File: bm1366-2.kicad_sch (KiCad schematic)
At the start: 73 parts, among them U1 25MHz, U13 BM1368_mode0, U15 TLV3544, U16 AP7331, U17 AP7331, U18 BM1368_mode0

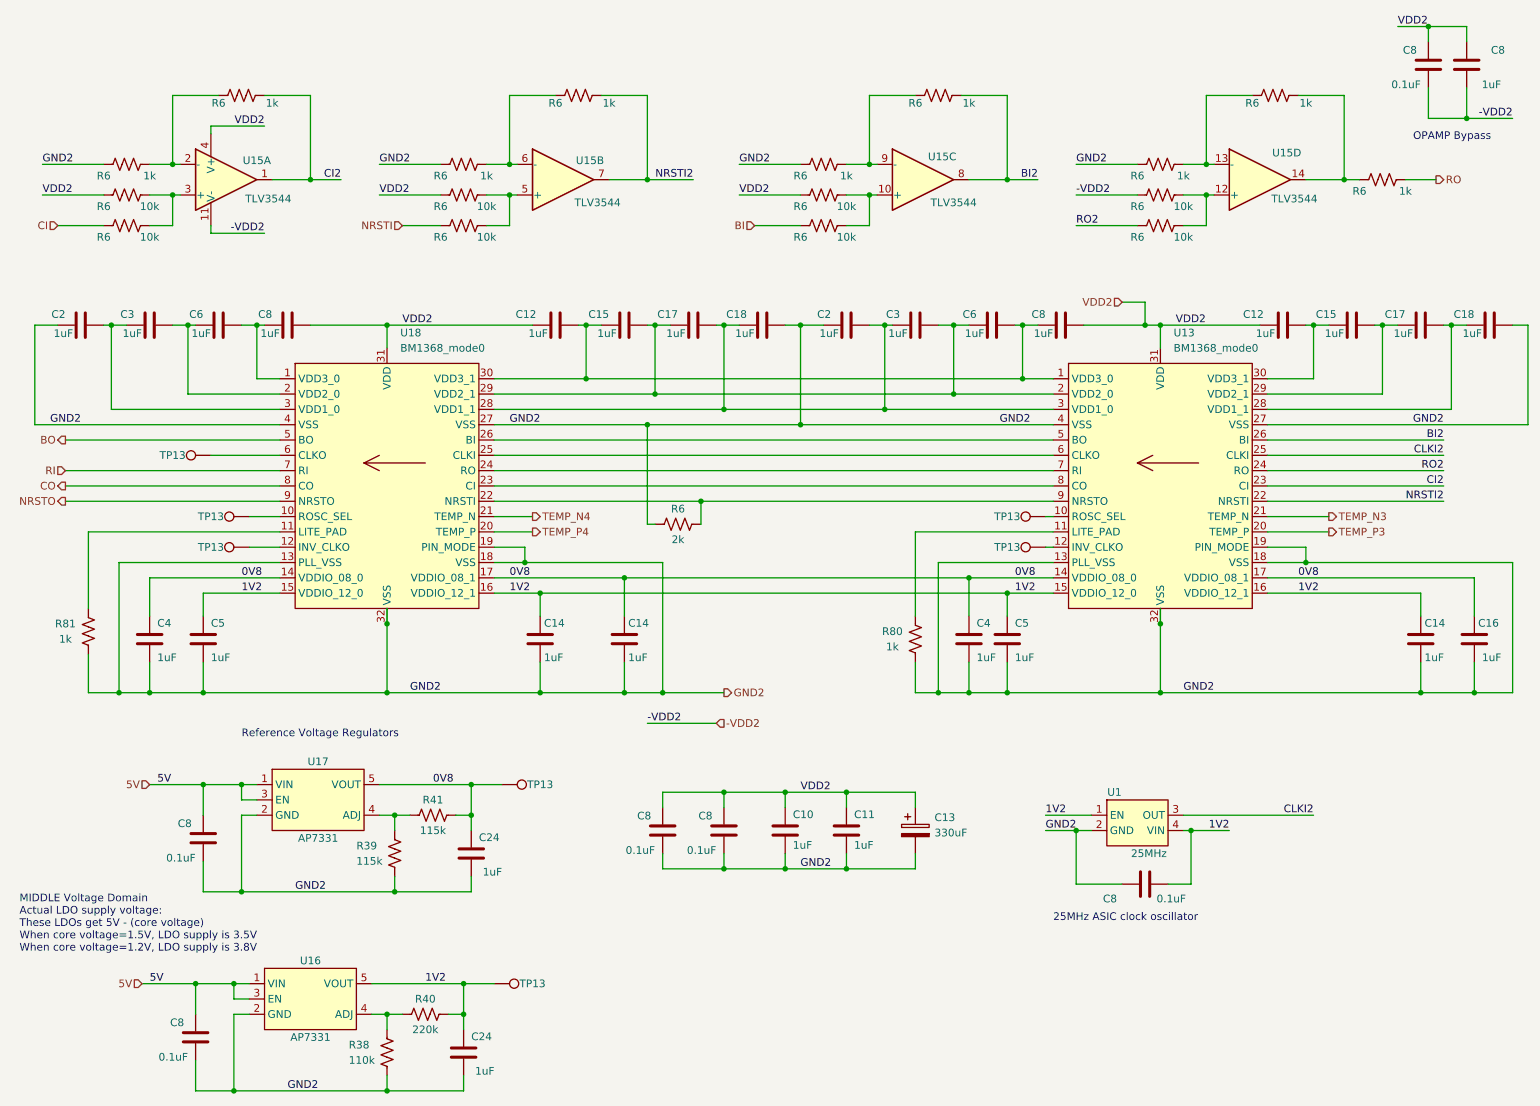
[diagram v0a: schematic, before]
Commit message: -Reset to 1V8/0V8 setup -Add TVS protection
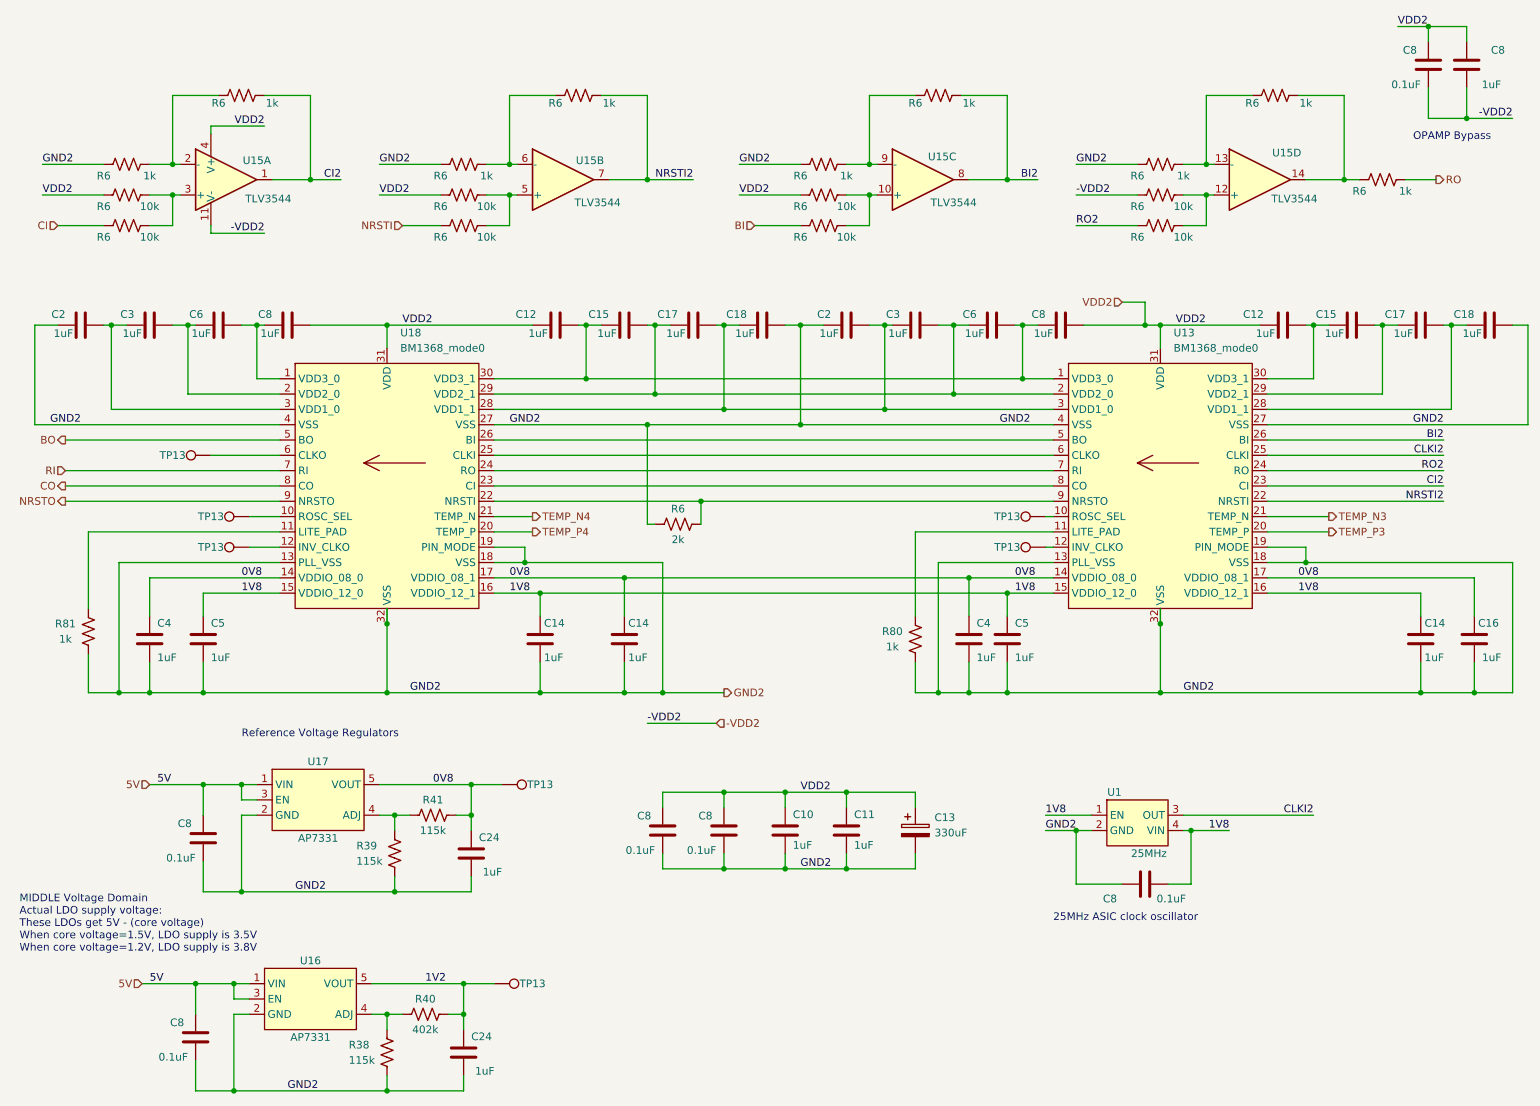
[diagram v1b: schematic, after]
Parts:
- R38: value 110k -> 115k; DK 311-110KLRTR-ND -> YAG2956CT-ND; PARTNO RC0402FR-07110KL -> RC0402FR-07115KL
- R40: value 220k -> 402k; DK 311-220KLRTR-ND -> YAG3151CT-ND; PARTNO RC0402FR-07220KL -> RC0402FR-07402KL
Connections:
- net 1V2: no longer C14.1, C14.1, C5.1, C5.1, C8.1, U1.1 (EN), U1.4 (VIN), U13.15 (VDDIO_12_0), U13.16 (VDDIO_12_1), U18.15 (VDDIO_12_0), U18.16 (VDDIO_12_1)
- new net 1V8: C14.1, C14.1, C5.1, C5.1, C8.1, U1.1 (EN), U1.4 (VIN), U13.15 (VDDIO_12_0), U13.16 (VDDIO_12_1), U18.15 (VDDIO_12_0), U18.16 (VDDIO_12_1)
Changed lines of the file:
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@@
 		)
 	)
-	(label "1V2"
+	(label "1V8"
 		(at 97.79 111.76 0)
 		(fields_autoplaced yes)
@@
 		)
 	)
-	(label "1V2"
+	(label "1V8"
 		(at 217.17 151.13 180)
 		(fields_autoplaced yes)
@@
 		)
 	)
-	(label "1V2"
+	(label "1V8"
 		(at 186.69 148.59 0)
 		(fields_autoplaced yes)
@@
 		)
 	)
-	(label "1V2"
+	(label "1V8"
 		(at 228.6 111.76 0)
 		(fields_autoplaced yes)
@@
 		)
 	)
-	(label "1V2"
+	(label "1V8"
 		(at 53.34 111.76 0)
 		(fields_autoplaced yes)
@@
 		)
 	)
-	(label "1V2"
+	(label "1V8"
 		(at 181.61 111.76 0)
 		(fields_autoplaced yes)
@@
 			)
 		)
-		(property "Value" "110k"
+		(property "Value" "115k"
 			(at 71.12 189.23 0)
 			(effects
@@
 			)
 		)
-		(property "DK" "311-110KLRTR-ND"
+		(property "DK" "YAG2956CT-ND"
 			(at 77.47 187.96 0)
 			(effects
@@
 			)
 		)
-		(property "PARTNO" "RC0402FR-07110KL"
+		(property "PARTNO" "RC0402FR-07115KL"
 			(at 77.47 187.96 0)
 			(effects
@@
 			)
 		)
-		(property "Value" "220k"
+		(property "Value" "402k"
 			(at 83.82 184.15 90)
 			(effects
@@
 			)
 		)
-		(property "DK" "311-220KLRTR-ND"
+		(property "DK" "YAG3151CT-ND"
 			(at 83.82 181.61 0)
 			(effects
@@
 			)
 		)
-		(property "PARTNO" "RC0402FR-07220KL"
+		(property "PARTNO" "RC0402FR-07402KL"
 			(at 83.82 181.61 0)
 			(effects

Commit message: updated to KiCad v9, filled in incomplete BOM and exported.
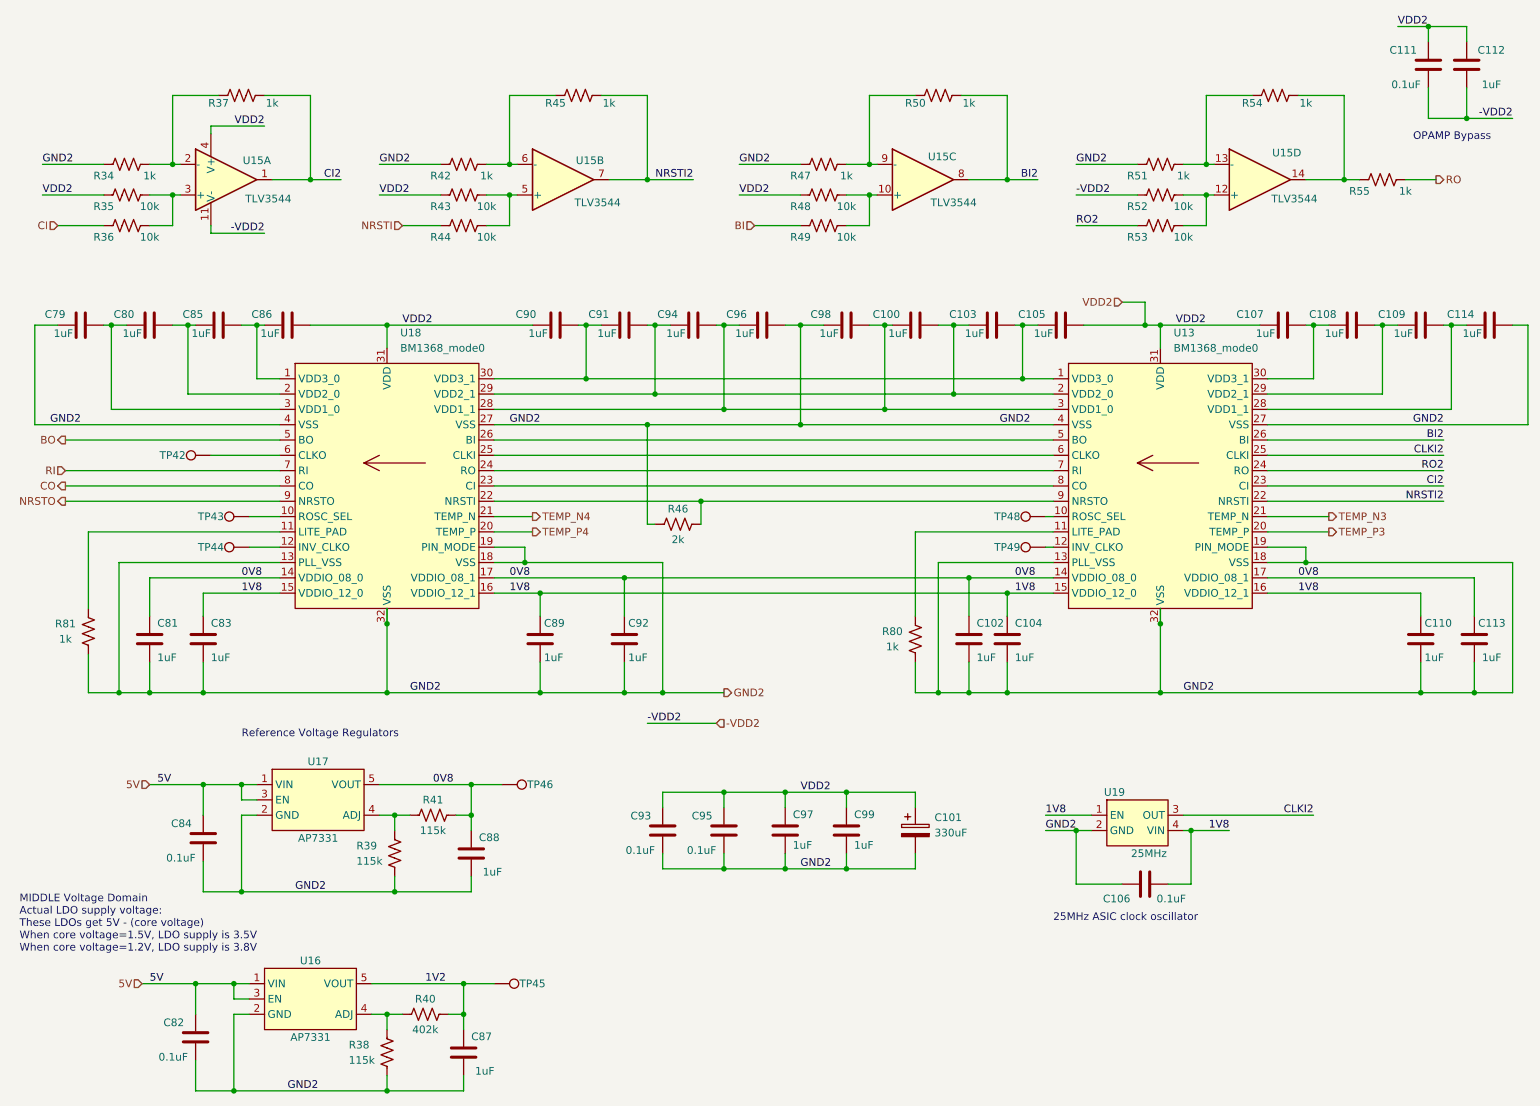
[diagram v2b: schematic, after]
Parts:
- renumbered C3 to C100, C13 to C101, C4 to C102, C6 to C103, C5 to C104, C8 to C105, C8 to C106, C12 to C107, C15 to C108, C17 to C109, C14 to C110, C8 to C111, C8 to C112, C16 to C113, C18 to C114, C2 to C79, C3 to C80, C4 to C81, C8 to C82, C5 to C83, C8 to C84, C6 to C85, C8 to C86, C24 to C87, C24 to C88, C14 to C89, C12 to C90, C15 to C91, C14 to C92, C8 to C93, C17 to C94, C8 to C95, C18 to C96, C10 to C97, C2 to C98, C11 to C99, R6 to R34, R6 to R35, R6 to R36, R6 to R37, R6 to R42, R6 to R43, R6 to R44, R6 to R45, R6 to R46, R6 to R47, R6 to R48, R6 to R49, R6 to R50, R6 to R51, R6 to R52, R6 to R53, R6 to R54, R6 to R55, TP13 to TP42, TP13 to TP43, TP13 to TP44, TP13 to TP45, TP13 to TP46, TP13 to TP48, TP13 to TP49, U1 to U19
